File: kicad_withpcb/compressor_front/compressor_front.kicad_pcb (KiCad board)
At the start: 2 copper layers, 35 x 110 mm, 33 parts, among them J1 MAIN BOARD, SW1 BYPASS, SW2 INT/EXT, SW3 HPF DEFEAT, SW4 LINK, U10 LM3915, U9 LM3914

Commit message: Use 100k pots for RV3 and RV6, and steady the sidechain high-pass
RK09K pots stop at 100k. RV3 becomes 100kA with R35 1k and R36 82k,
which scales the threshold network and keeps the -20 to +20 dBu range.
RV6 becomes 100k, so the slowest release drops to about 0.4 s.

R35 at 2k4 had also loaded the sidechain high-pass (C14 into R38), so at
the lowest threshold its corner rose to about 400 Hz. R38 1k and C14 2u2
hold it between about 80 and 160 Hz across the threshold knob.
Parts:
- RV3: value 250kA -> 100kA
- RV6: value 500k -> 100k
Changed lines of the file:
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@@
 			)
 		)
-		(property "Value" "500k"
+		(property "Value" "100k"
 			(at 6.05 10.15 90)
 			(layer "F.Fab")
@@
 			)
 		)
-		(property "Value" "250kA"
+		(property "Value" "100kA"
 			(at 6.05 10.15 90)
 			(layer "F.Fab")

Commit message: Put RV6 back to 500k, to be a Bourns PTV09
RK09K stops at 100k, which would cut the slowest release to about 0.4 s.
Lyn chose a 500k Bourns PTV09 instead, keeping it near 1.8 s.
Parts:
- RV6: value 100k -> 500k
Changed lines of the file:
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@@
 			)
 		)
-		(property "Value" "100k"
+		(property "Value" "500k"
 			(at 6.05 10.15 90)
 			(layer "F.Fab")

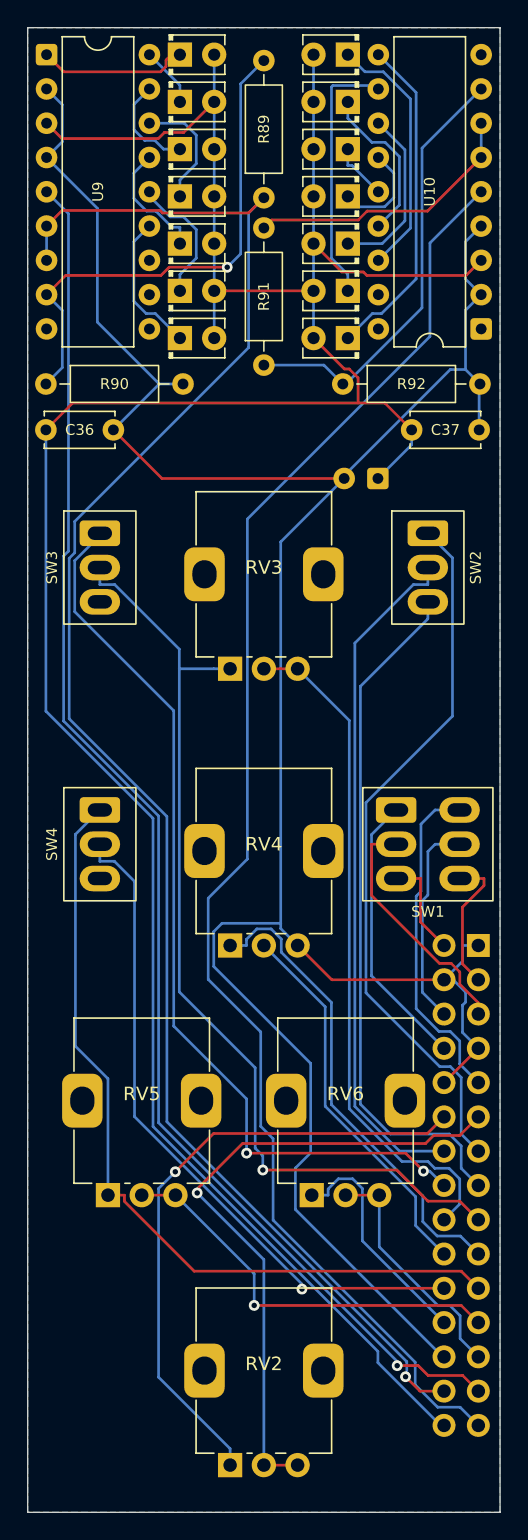
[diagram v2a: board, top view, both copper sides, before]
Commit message: Swap the front panel toggles for Altronics' Salecom mini toggles
BYPASS is now an S1350 (DPDT) and KEY, HPF and LINK are S1315 (SPDT);
the S1332 centre-off shares the SPDT footprint. Footprints and STEP
models follow the drawings on the Altronics product pages: pins on
4.70 mm with 1.3 mm holes, DPDT rows 4.83 mm apart, bodies 6.9 or 11.4
by 12.7 mm standing 10.4 mm off the board, 1/4-40 bushing 8.9 mm long.

The toggles move 0.25 mm inboard (x 7.15 / 30.95) so the S1350 body
stays on the 35 mm board, and the pot courtyard is trimmed to its pads
so it doesn't overlap the S1350. C38 moves 1 mm up, clear of the SW2
body. The switch nets and the nets crowding J1 were re-routed with
Freerouting: DRC 0 errors, 0 unconnected, schematic parity clean.

The panel's toggle holes go from 5.2 to 6.5 mm, and make_panel.py now
checks the switch and pot bodies behind the panel against each other
and the front board. The board now sits about 10.6 mm behind the panel,
set by the 9 mm pots; the toggles' long bushing no longer needs a
thinned panel, but the pots' 5 mm one does.
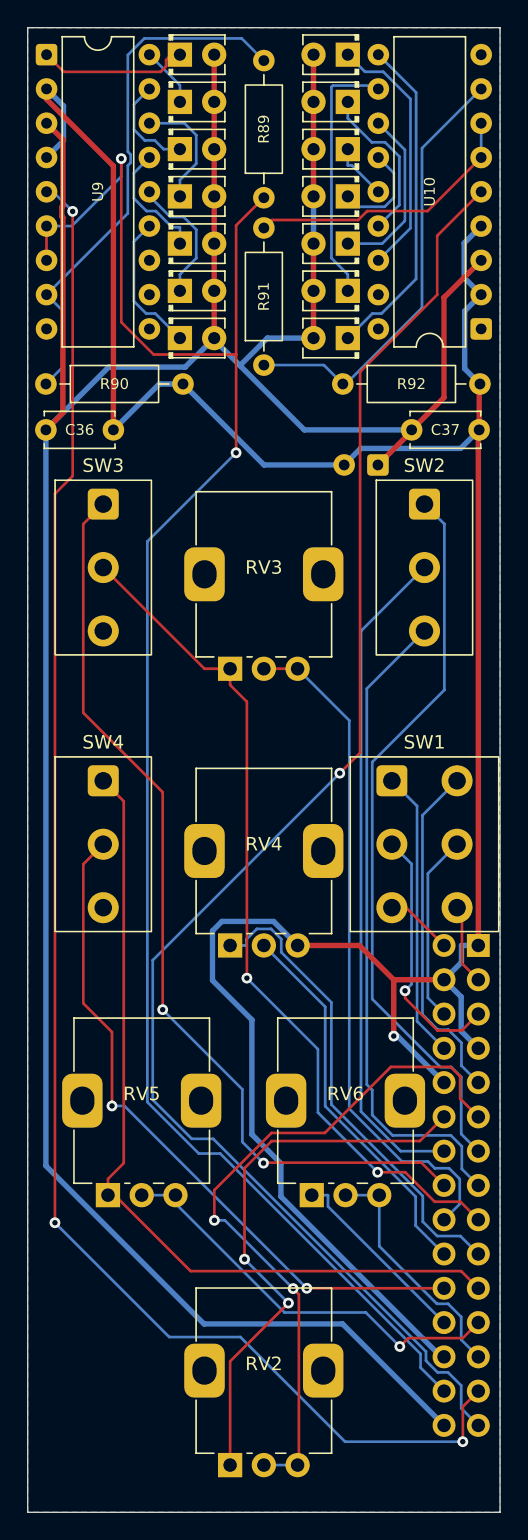
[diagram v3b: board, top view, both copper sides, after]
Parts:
- SW1: footprint compressor_front:SW_Toggle_SubMini_DPDT_Jaycar_ST0310 -> compressor_front:SW_Toggle_Mini_DPDT_Salecom_S1350
- SW2, SW3, SW4: footprint compressor_front:SW_Toggle_SubMini_SPDT_Jaycar_ST0300 -> compressor_front:SW_Toggle_Mini_SPDT_Salecom_S1315
- moved C38 1.00 mm to (127.5, 84.4)
- moved SW1 0.25 mm to (130.9, 112.5)
- moved SW2 0.25 mm to (130.9, 92.0)
- moved SW3 0.25 mm to (107.2, 92.0)
- moved SW4 0.25 mm to (107.2, 112.5)
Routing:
- net GR_METER: track 104.8 -> 119.2 mm, vias 1 -> 3
- net +16V: track 203.1 -> 215.2 mm
- net AGND: track 189.2 -> 198.7 mm, vias 0 -> 1
- net HPF_B: track 71.5 -> 63.3 mm, vias 1 -> 2
- net GR_REF: track 126.7 -> 134.6 mm, vias 1 -> 2
- net MAKEUP_FB: track 46.0 -> 41.5 mm, vias 1 -> 2
- net IN-: track 10.5 -> 5.99 mm
- net LVL_METER: track 109.0 -> 112.9 mm, vias 0 -> 1
- net OUT-A: track 48.0 -> 51.8 mm, vias 1 -> 2
- net TIMING: track 17.3 -> 14.2 mm
- net KEY: track 51.5 -> 48.8 mm
- net IN+: track 7.49 -> 5.02 mm
- net OUT-: track 15.4 -> 14.0 mm
- net HPF_A: track 67.6 -> 69.1 mm
- net LINK_SW: track 60.9 -> 62.3 mm
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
